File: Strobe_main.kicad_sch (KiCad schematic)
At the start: 0 parts

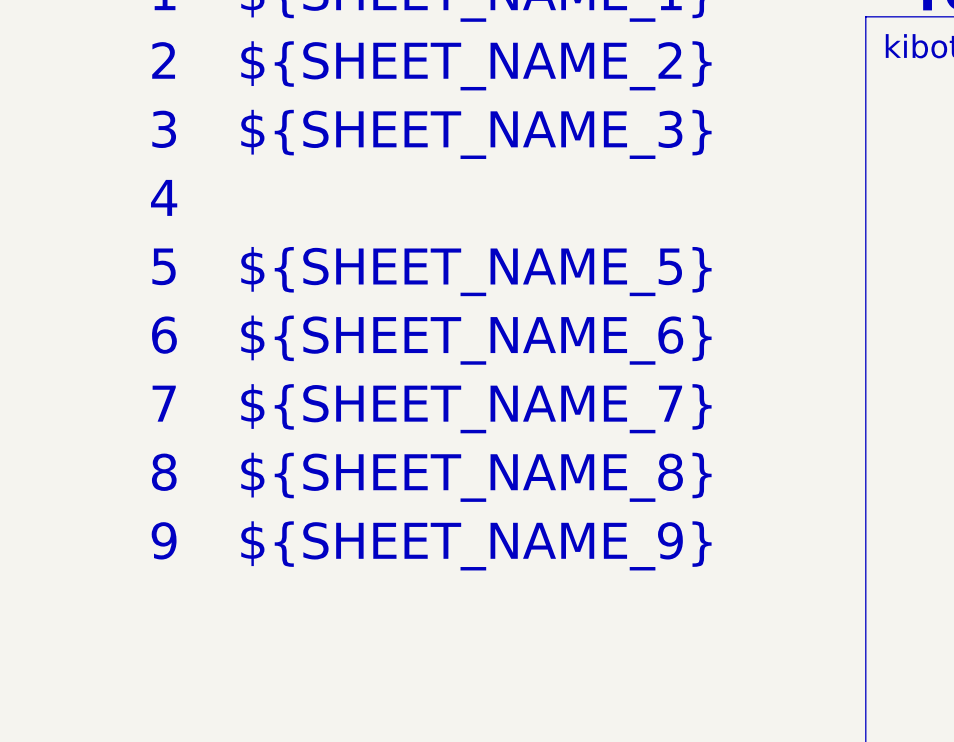
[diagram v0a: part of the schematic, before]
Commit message: Updated C22 and C23
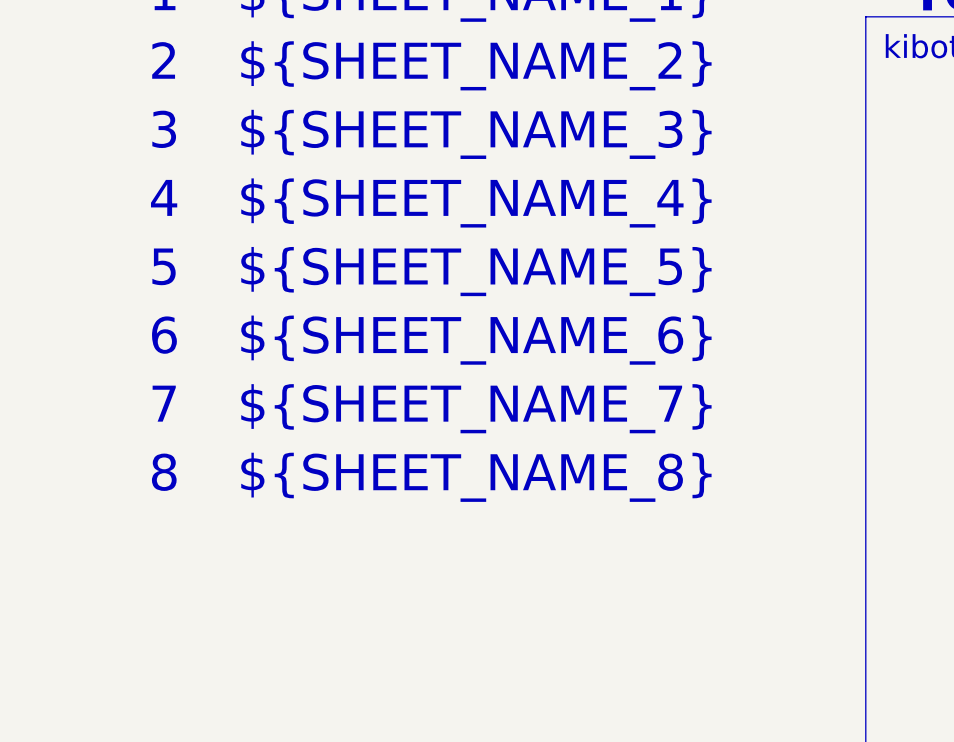
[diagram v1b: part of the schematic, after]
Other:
- note added: "${SHEET_NAME_4}"
- note removed: "${SHEET_NAME_9}"
- note removed: "9"
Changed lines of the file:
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@@
+		)
+	)
+	(text "${SHEET_NAME_4}"
+		(exclude_from_sim no)
+		(at 38.1 86.36 0)
+		(effects
+			(font
+				(face "Times New Roman")
+				(size 4 4)
+				(color 0 0 0 1)
+			)
+			(justify left bottom)
+			(href "#4")
 		)
 	)
@@
 		)
 	)
-	(text "${SHEET_NAME_9}"
-		(exclude_from_sim no)
-		(at 38.1 124.46 0)
-		(effects
-			(font
-				(face "Times New Roman")
-				(size 4 4)
-				(color 0 0 0 1)
-			)
-			(justify left bottom)
-			(href "#9")
-		)
-	)
 	(text "8"
 		(exclude_from_sim no)
@@
 		)
 	)
-	(text "9"
-		(exclude_from_sim no)
-		(at 31.75 124.46 0)
-		(effects
-			(font
-				(face "Times New Roman")
-				(size 4 4)
-				(color 0 0 0 1)
-			)
-			(justify right bottom)
-			(href "#9")
-		)
-	)
